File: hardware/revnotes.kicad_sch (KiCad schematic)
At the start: 0 parts

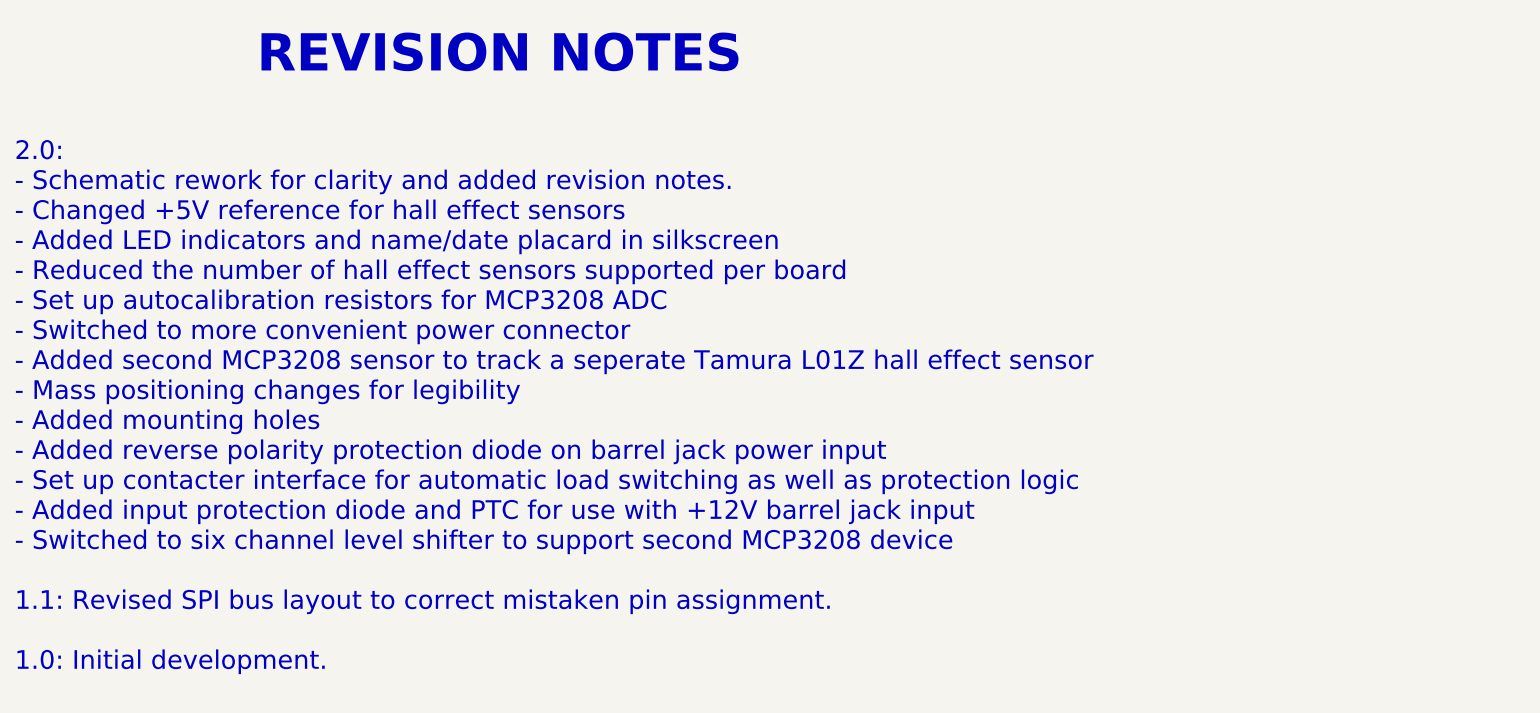
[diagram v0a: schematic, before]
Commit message: Edited schematic to relocated FETs as proper low-side switches
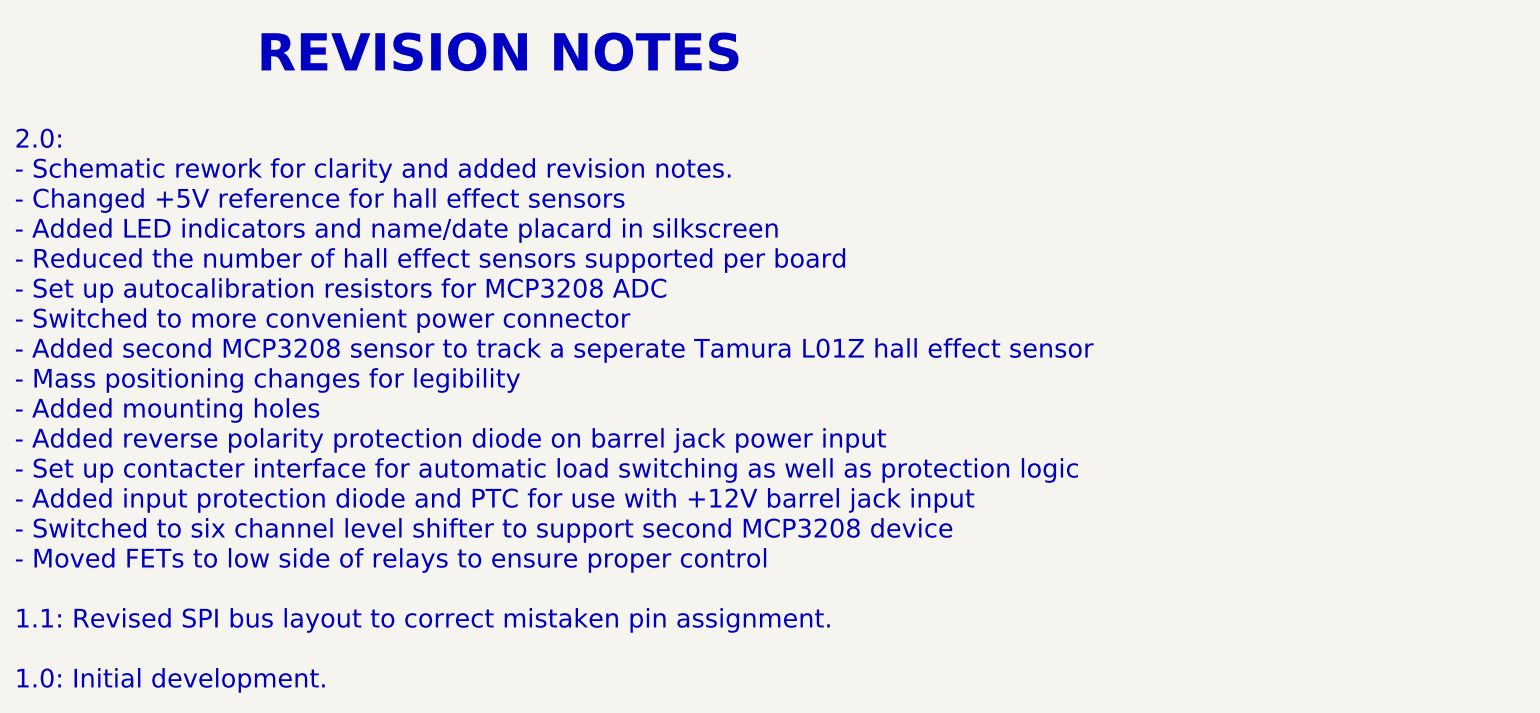
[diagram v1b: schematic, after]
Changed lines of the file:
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@@
     (comment 2 "(PENDING REVIEW)")
   )
-  (text "2.0: \n- Schematic rework for clarity and added revision notes.\n- Changed +5V reference for hall effect sensors\n- Added LED indicators and name/date placard in silkscreen\n- Reduced the number of hall effect sensors supported per board\n- Set up autocalibration resistors for MCP3208 ADC\n- Switched to more convenient power connector\n- Added second MCP3208 sensor to track a seperate Tamura L01Z hall effect sensor\n- Mass positioning changes for legibility\n- Added mounting holes\n- Added reverse polarity protection diode on barrel jack power input\n- Set up contacter interface for automatic load switching as well as protection logic\n- Added input protection diode and PTC for use with +12V barrel jack input\n- Switched to six channel level shifter to support second MCP3208 device\n\n1.1: Revised SPI bus layout to correct mistaken pin assignment.\n\n1.0: Initial development."
-    (at 83.82 119.38 0)
+  (text "2.0: \n- Schematic rework for clarity and added revision notes.\n- Changed +5V reference for hall effect sensors\n- Added LED indicators and name/date placard in silkscreen\n- Reduced the number of hall effect sensors supported per board\n- Set up autocalibration resistors for MCP3208 ADC\n- Switched to more convenient power connector\n- Added second MCP3208 sensor to track a seperate Tamura L01Z hall effect sensor\n- Mass positioning changes for legibility\n- Added mounting holes\n- Added reverse polarity protection diode on barrel jack power input\n- Set up contacter interface for automatic load switching as well as protection logic\n- Added input protection diode and PTC for use with +12V barrel jack input\n- Switched to six channel level shifter to support second MCP3208 device\n- Moved FETs to low side of relays to ensure proper control\n\n1.1: Revised SPI bus layout to correct mistaken pin assignment.\n\n1.0: Initial development."
+    (at 83.82 121.92 0)
     (effects (font (size 2.54 2.54)) (justify left bottom))
   )
